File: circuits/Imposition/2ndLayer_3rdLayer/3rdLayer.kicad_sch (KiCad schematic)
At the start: 30 parts, among them J3 Conn_02x10_Odd_Even, J4 USB_C_Receptacle_USB2.0, SW10 SW_DIP_x04, SW7 SW_SPST, SW8 SW_SPST, SW9 SW_SPST, U10 FT231XS, U9 Display_Akzk_128x68OLED

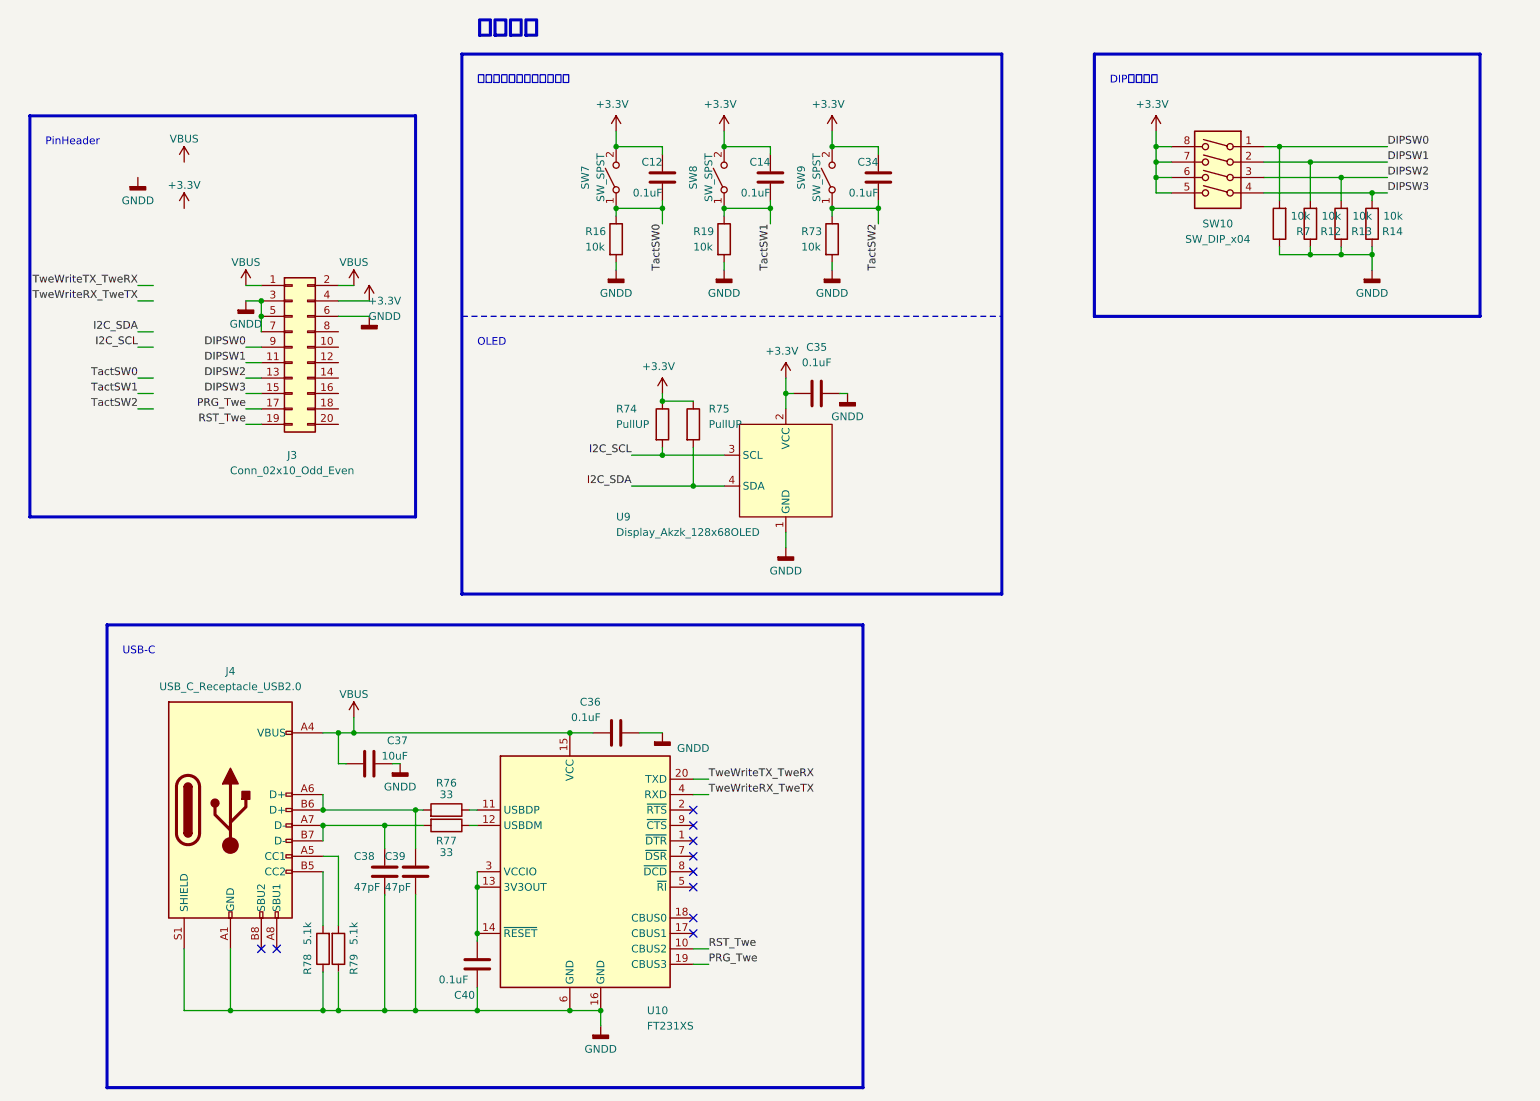
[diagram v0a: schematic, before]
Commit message: 発注_第一弾
Drive, 1stLayer_Power, 2ndLayer_3rdLayer
を発注
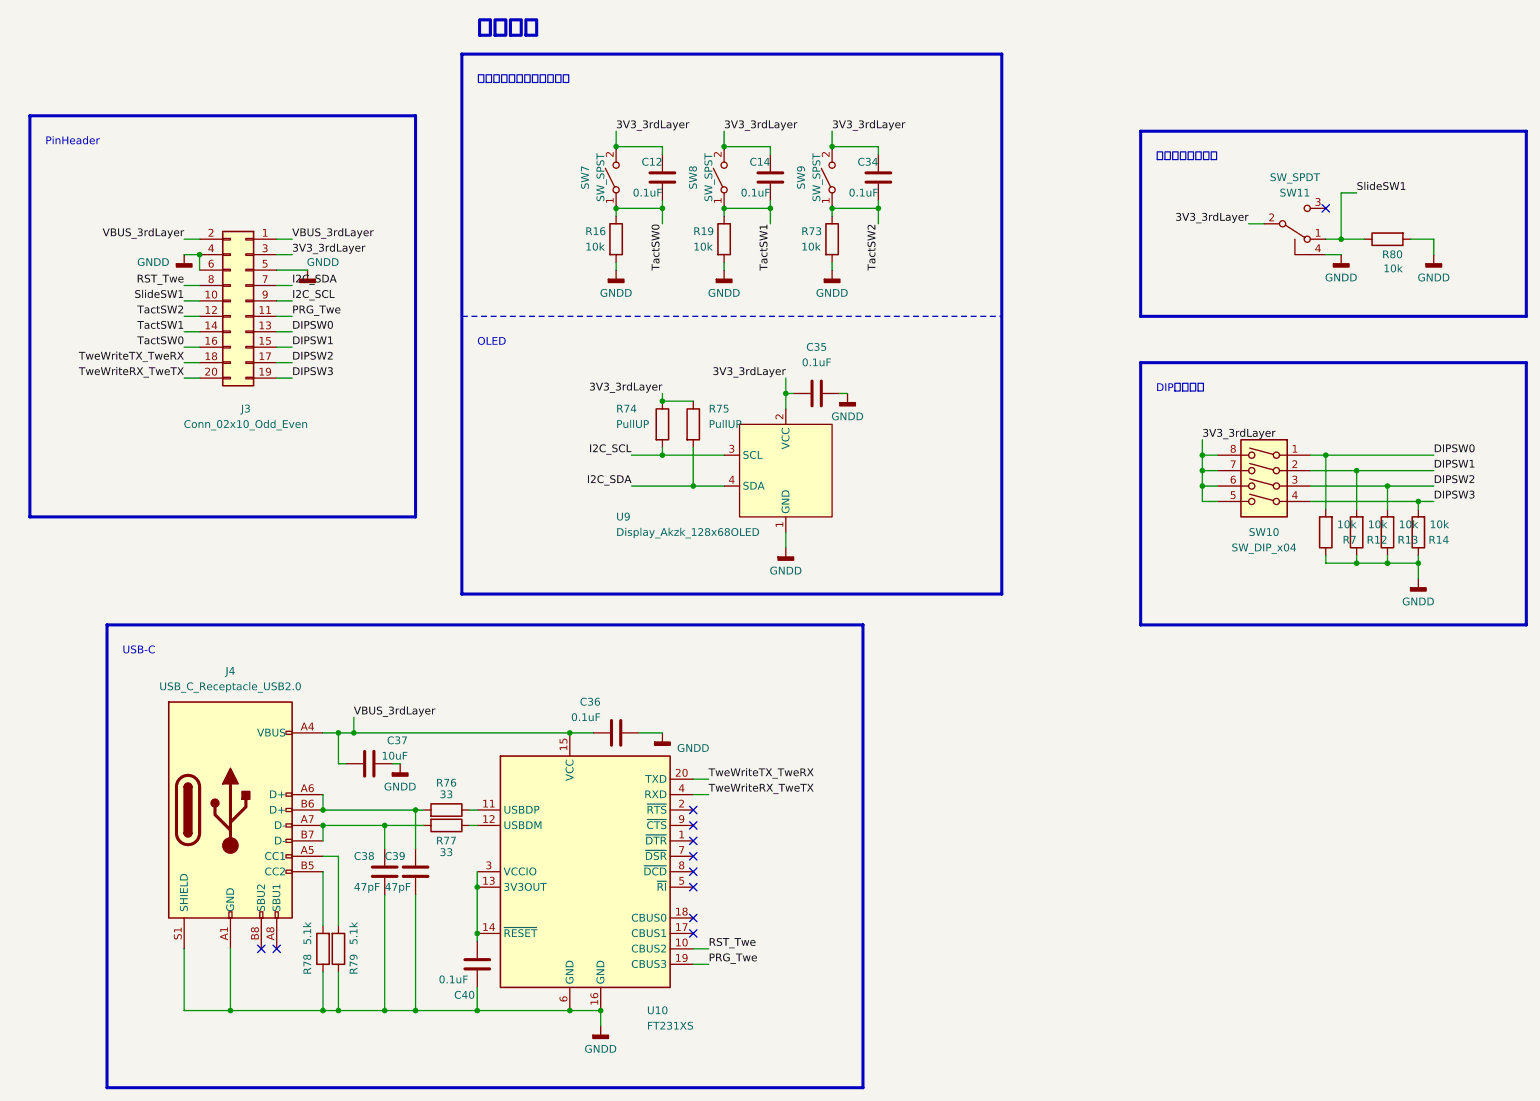
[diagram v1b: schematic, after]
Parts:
- added R80: 10k, Resistor_SMD:R_0402_1005Metric, symbol Device:R
- added SW11: SW_SPDT, TomoshibiLibrary:SW_Slide_DPDT_SSSS820101, symbol Switch:SW_SPDT
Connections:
- net DIPSW0: now also J3.13 (Pin_13); no longer J3.9 (Pin_9)
- net DIPSW1: now also J3.15 (Pin_15); no longer J3.11 (Pin_11)
- net DIPSW2: now also J3.17 (Pin_17); no longer J3.13 (Pin_13)
- net DIPSW3: now also J3.19 (Pin_19); no longer J3.15 (Pin_15)
- net GNDD: now also J3.4 (Pin_4), R80.2, SW11.4 (shell), SW11.5 (shell), SW11.6 (shell), SW11.G1 (shell), SW11.G2 (shell), SW11.G3 (shell), SW11.G4 (shell); no longer J3.3 (Pin_3), J3.7 (Pin_7)
- net I2C_SCL: now also J3.9 (Pin_9)
- net I2C_SDA: now also J3.7 (Pin_7)
- net PRG_Twe: now also J3.11 (Pin_11); no longer J3.17 (Pin_17)
- net RST_Twe: now also J3.8 (Pin_8); no longer J3.19 (Pin_19)
- net TactSW0: now also J3.16 (Pin_16)
- net TactSW1: now also J3.14 (Pin_14)
- net TactSW2: now also J3.12 (Pin_12)
- net TweWriteRX_TweTX: now also J3.20 (Pin_20)
- net TweWriteTX_TweRX: now also J3.18 (Pin_18)
- net SlideSW1: now reaches J3.10 (Pin_10)
- net SlideSW1: now also R80.1, SW11.1 (A)
- net +3.3V renamed 3V3_3rdLayer
- net 3V3_3rdLayer: now also J3.3 (Pin_3), SW11.2 (B); no longer J3.4 (Pin_4)
- net VBUS renamed VBUS_3rdLayer
- no-connect marks 10 -> 11
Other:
- note added: "スライドスイッチ"
- moved on the sheet: J3, R12, R13, R14, R7, SW10
